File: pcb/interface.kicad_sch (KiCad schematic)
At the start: 9 parts, among them J0 UJ20-C-H-G-SMT-P16-TR

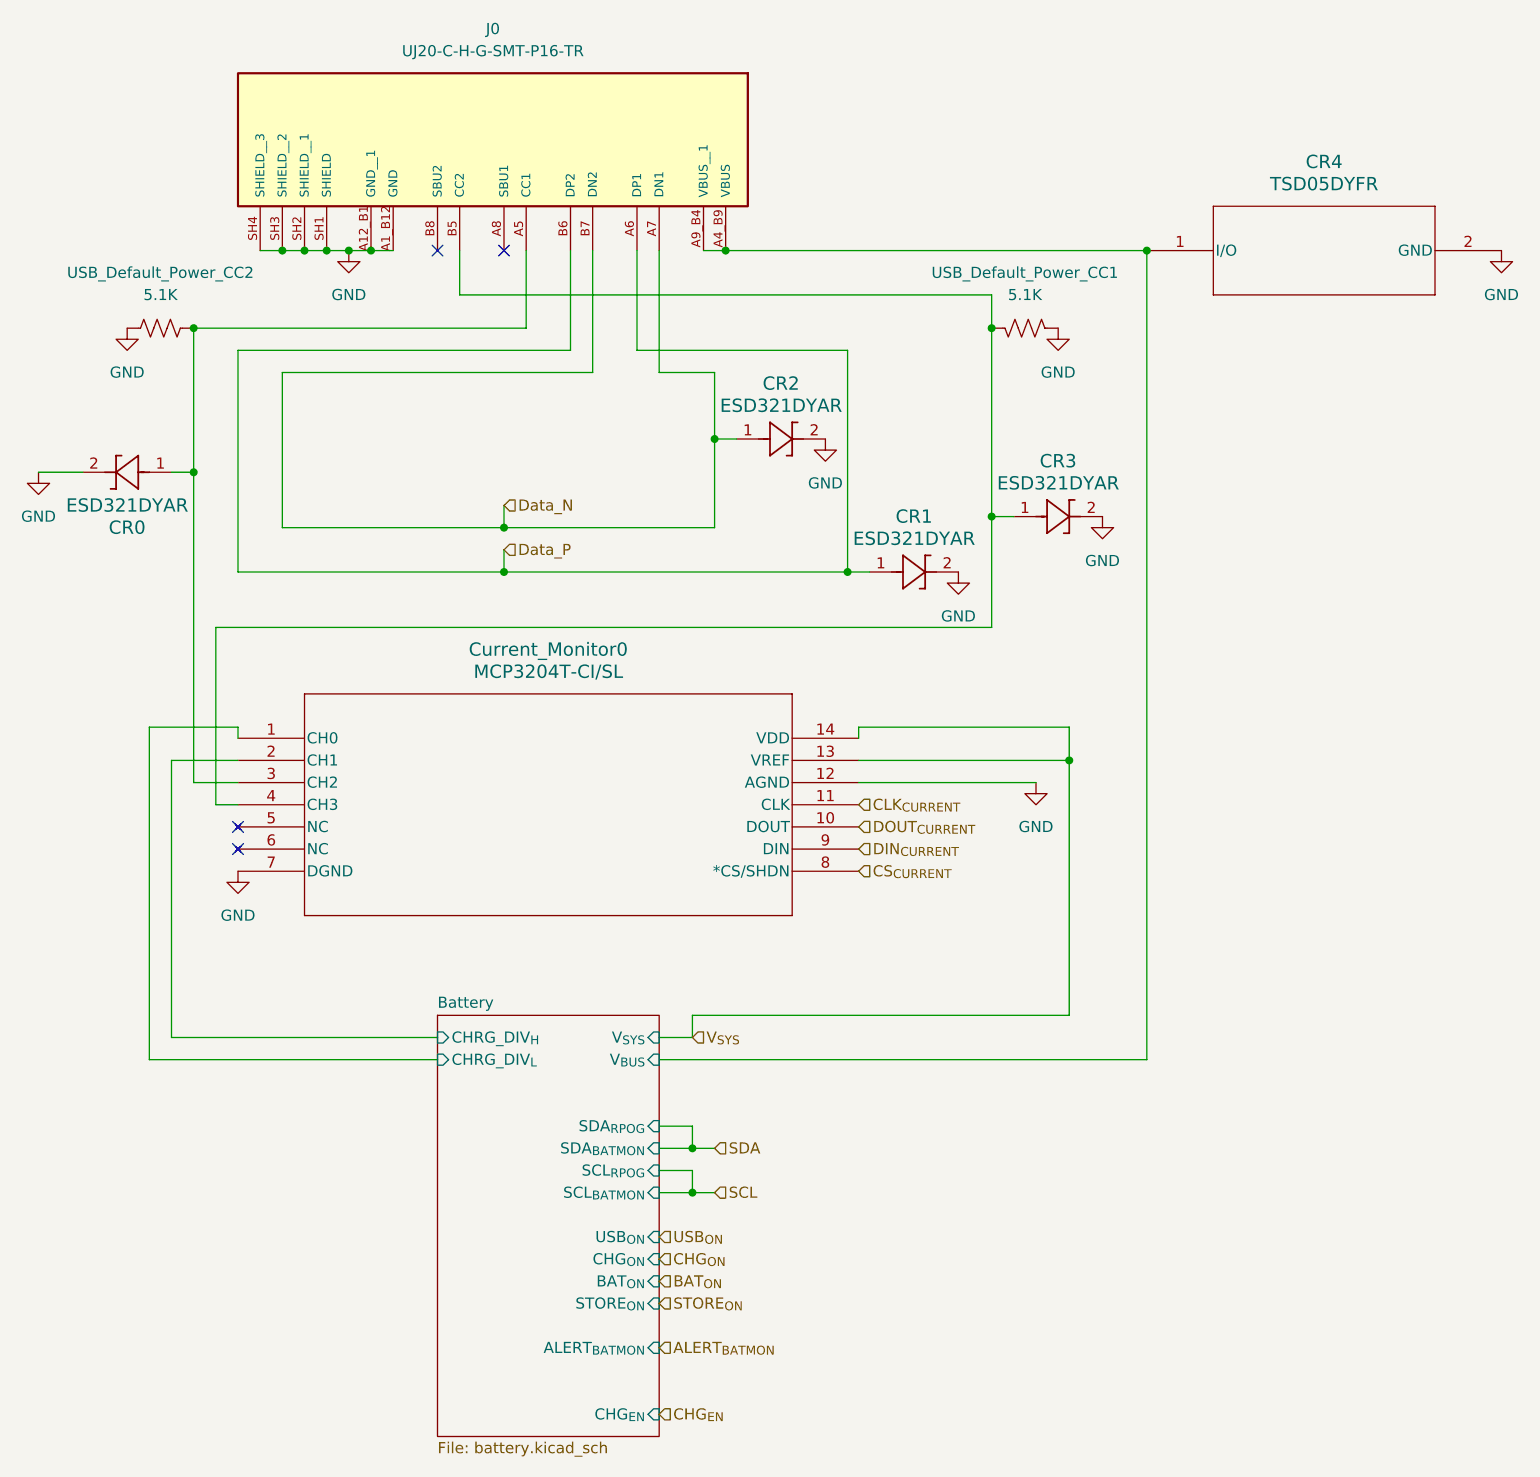
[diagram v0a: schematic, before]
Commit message: Add more ESD protection
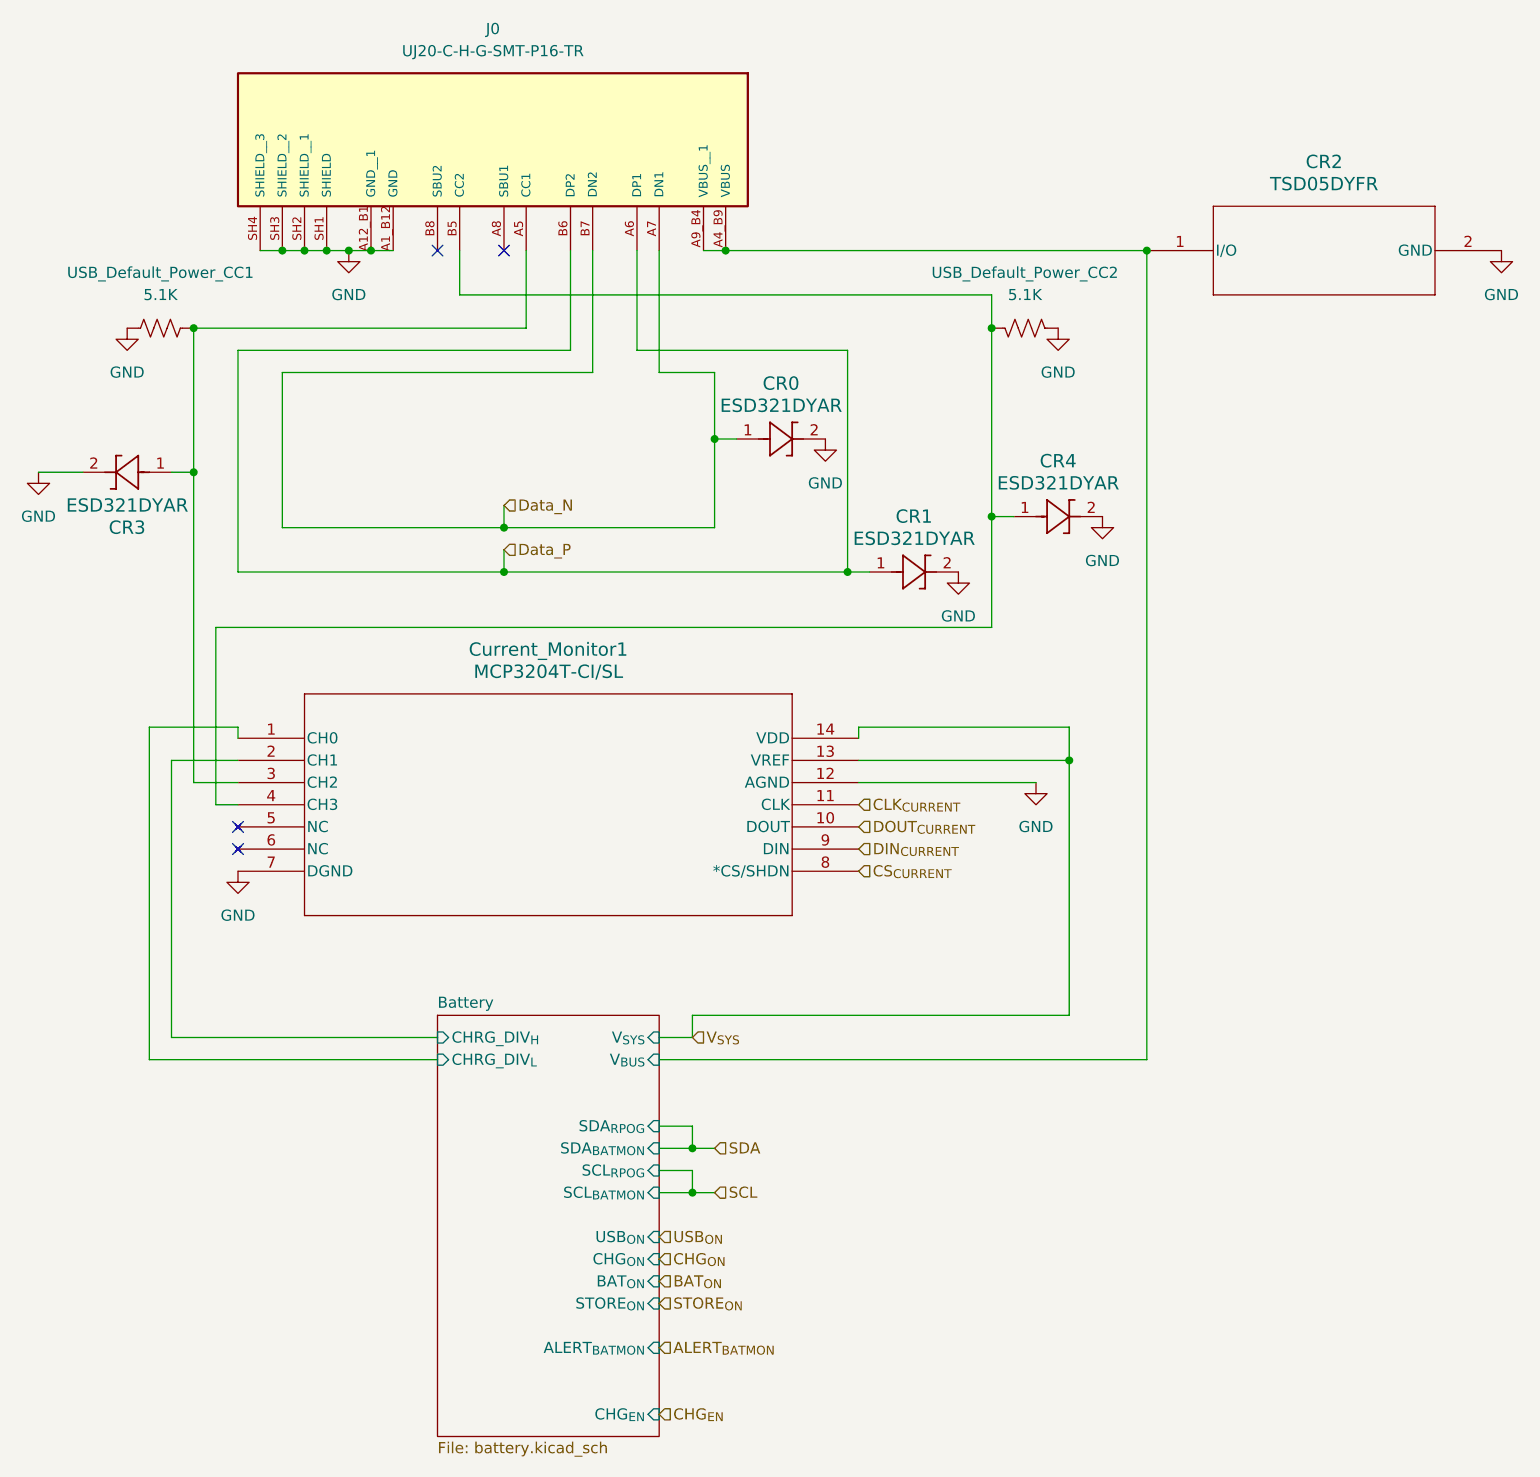
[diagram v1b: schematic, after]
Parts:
- renumbered CR2 to CR0, CR4 to CR2, CR0 to CR3, CR3 to CR4, Current_Monitor0 to Current_Monitor1, USB_Default_Power_CC2 to USB_Default_Power_CC1, USB_Default_Power_CC1 to USB_Default_Power_CC2
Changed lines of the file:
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@@
 	(title_block
 		(title "Stenoswitch")
-		(rev "0.1")
+		(date "2025-10-21")
+		(rev "0.3")
 		(company "https://github.com/Bennett-Petzold/port_plover")
 		(comment 1 "NO WARRANTY. See license.")
@@
 		(dnp no)
 		(fields_autoplaced yes)
-		(property "Reference" "#PWR07"
+		(property "Reference" "#PWR09"
 			(at 179.07 76.2 0)
 			(effects
@@
 		(dnp no)
 		(fields_autoplaced yes)
-		(property "Reference" "USB_Default_Power_CC2"
+		(property "Reference" "USB_Default_Power_CC1"
 			(at 102.87 50.8 90)
 			(effects
@@
 		(dnp no)
 		(fields_autoplaced yes)
-		(property "Reference" "#PWR037"
+		(property "Reference" "#PWR023"
 			(at 256.54 54.61 0)
 			(effects
@@
 		(dnp no)
 		(fields_autoplaced yes)
-		(property "Reference" "#PWR08"
+		(property "Reference" "#PWR021"
 			(at 194.31 91.44 0)
 			(effects
@@
 		(dnp no)
 		(fields_autoplaced yes)
-		(property "Reference" "#PWR035"
+		(property "Reference" "#PWR027"
 			(at 88.9 80.01 0)
 			(effects
@@
 		(dnp no)
 		(fields_autoplaced yes)
-		(property "Reference" "CR0"
+		(property "Reference" "CR3"
 			(at 99.06 80.01 0)
 			(effects
@@
 		(dnp no)
 		(fields_autoplaced yes)
-		(property "Reference" "#PWR04"
+		(property "Reference" "#PWR0105"
 			(at 111.76 125.73 0)
 			(effects
@@
 		(dnp no)
 		(fields_autoplaced yes)
-		(property "Reference" "CR4"
+		(property "Reference" "CR2"
 			(at 236.22 38.1 0)
 			(effects
@@
 		(on_board yes)
 		(dnp no)
-		(property "Reference" "Current_Monitor0"
+		(property "Reference" "Current_Monitor1"
 			(at 147.32 93.98 0)
 			(effects
@@
 		(dnp no)
 		(fields_autoplaced yes)
-		(property "Reference" "#PWR03"
+		(property "Reference" "#PWR0101"
 			(at 205.74 63.5 0)
 			(effects
@@
 		(dnp no)
 		(fields_autoplaced yes)
-		(property "Reference" "CR3"
+		(property "Reference" "CR4"
 			(at 205.74 72.39 0)
 			(effects
@@
 		(dnp no)
 		(fields_autoplaced yes)
-		(property "Reference" "#PWR05"
+		(property "Reference" "#PWR0102"
 			(at 203.2 115.57 0)
 			(effects
@@
 		(dnp no)
 		(fields_autoplaced yes)
-		(property "Reference" "#PWR0104"
+		(property "Reference" "#PWR0106"
 			(at 124.46 54.61 0)
 			(effects
@@
 		(dnp no)
 		(fields_autoplaced yes)
-		(property "Reference" "#PWR02"
+		(property "Reference" "#PWR0104"
 			(at 99.06 63.5 0)
 			(effects
@@
 		(dnp no)
 		(fields_autoplaced yes)
-		(property "Reference" "CR2"
+		(property "Reference" "CR0"
 			(at 173.99 63.5 0)
 			(effects
@@
 		(dnp no)
 		(fields_autoplaced yes)
-		(property "Reference" "#PWR036"
+		(property "Reference" "#PWR028"
 			(at 210.82 85.09 0)
 			(effects
@@
 		(dnp no)
 		(fields_autoplaced yes)
-		(property "Reference" "USB_Default_Power_CC1"
+		(property "Reference" "USB_Default_Power_CC2"
 			(at 201.93 50.8 90)
 			(effects
